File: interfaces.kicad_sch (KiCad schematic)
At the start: 125 parts, among them J3 USB-Micro-B_Amphenol_10118192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, J6 PinHeader_2x7_P2mm_Drill0.9mm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, J7 PinHeader_1x6_P2.54mm_Drill1.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, U1 MTFC16GAPALNA-AIT, U14 XC7A100T-FGG484, U17 USB3300-EZK-TR, U18 USB3300-EZK-TR, U19 FT4232H_QFN, U21 LSF0108RKSR, U22 LSF0101DRYR, U23 Oscillator_24MHz_ASEMB, U24 Oscillator_24MHz_ASEMB, U6 NVT2008BQ,115, Y1 Resonator_12MHz_ABM8G

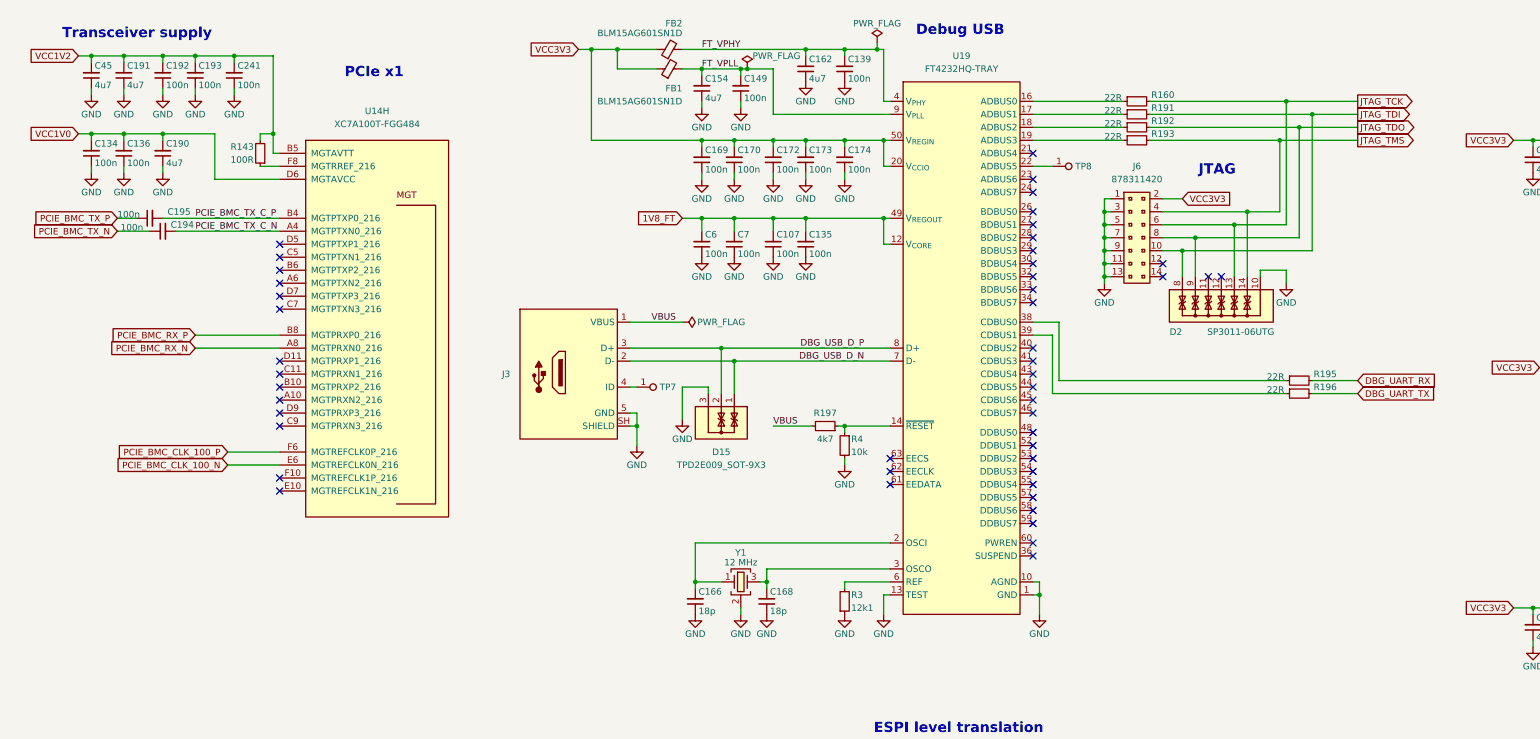
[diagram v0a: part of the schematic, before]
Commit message: [#68236] Update symbols and footprints, clean ERC and DRC
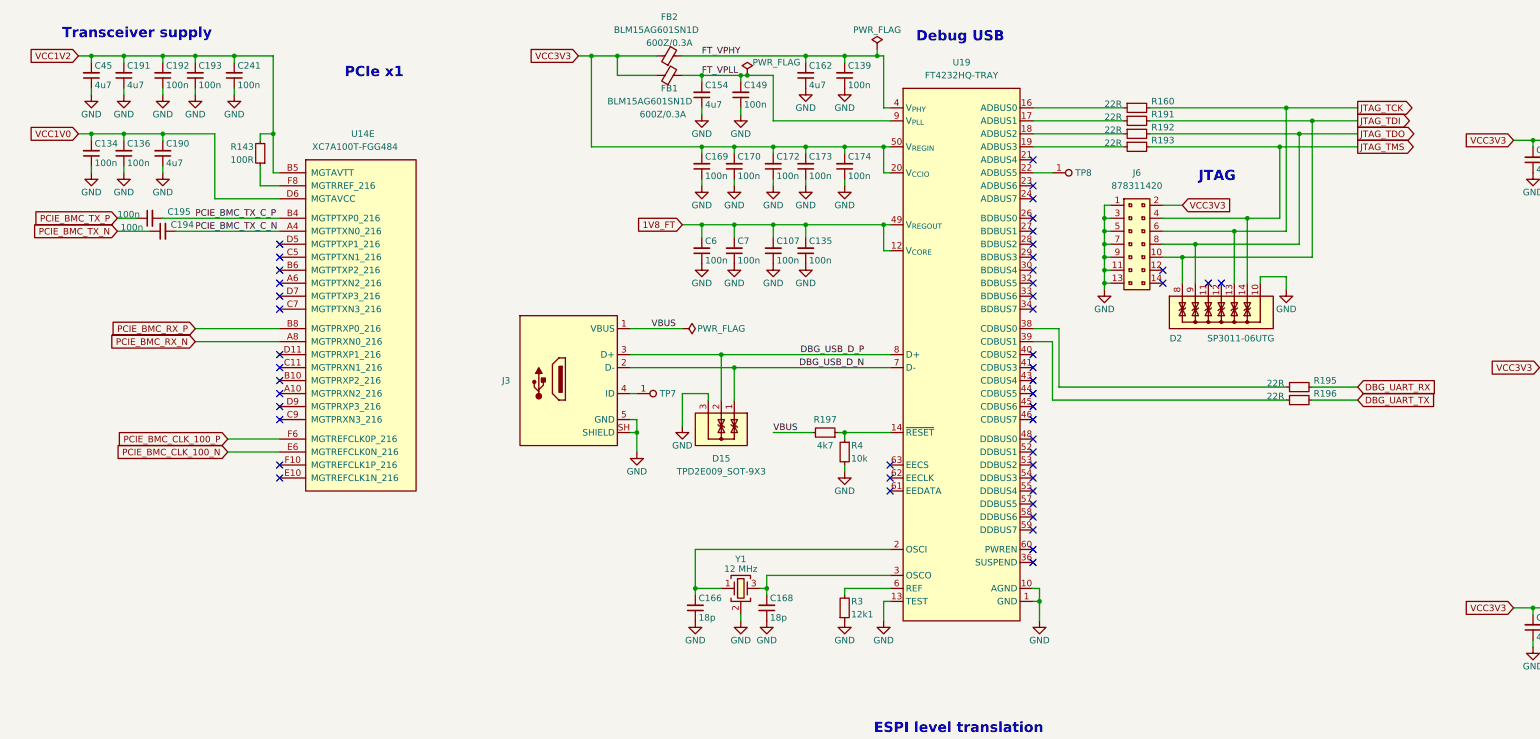
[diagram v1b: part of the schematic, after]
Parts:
- C134, C136, C17, C186, C187, C189, C192, C193, C194, C195, C223, C224, C229, C230, C231, C232, C241, C39: Public (none) -> False
- FB1, FB2: Val (none) -> 600Z/0.3A
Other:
- moved on the sheet: C107, C135, C139, C149, C154, C162, C166, C168, C169, C170, C172, C173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

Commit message: [#82378] Project refresh 81589
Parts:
- U21: DNP DNP -> (none)
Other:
- moved on the sheet: C4, C5

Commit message: pcb layout progress
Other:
- note added: "SFEM016GB1ED1TO-I-5E-311-STD (Drop in Replacement)"
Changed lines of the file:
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@@
 		(rev "1.1.3")
+	)
+	(text "SFEM016GB1ED1TO-I-5E-311-STD (Drop in Replacement)\n"
+		(exclude_from_sim no)
+		(at 89.154 227.33 0)
+		(effects
+			(font
+				(size 1.27 1.27)
+			)
+		)
 	)
 	(text "USB CLIENT"

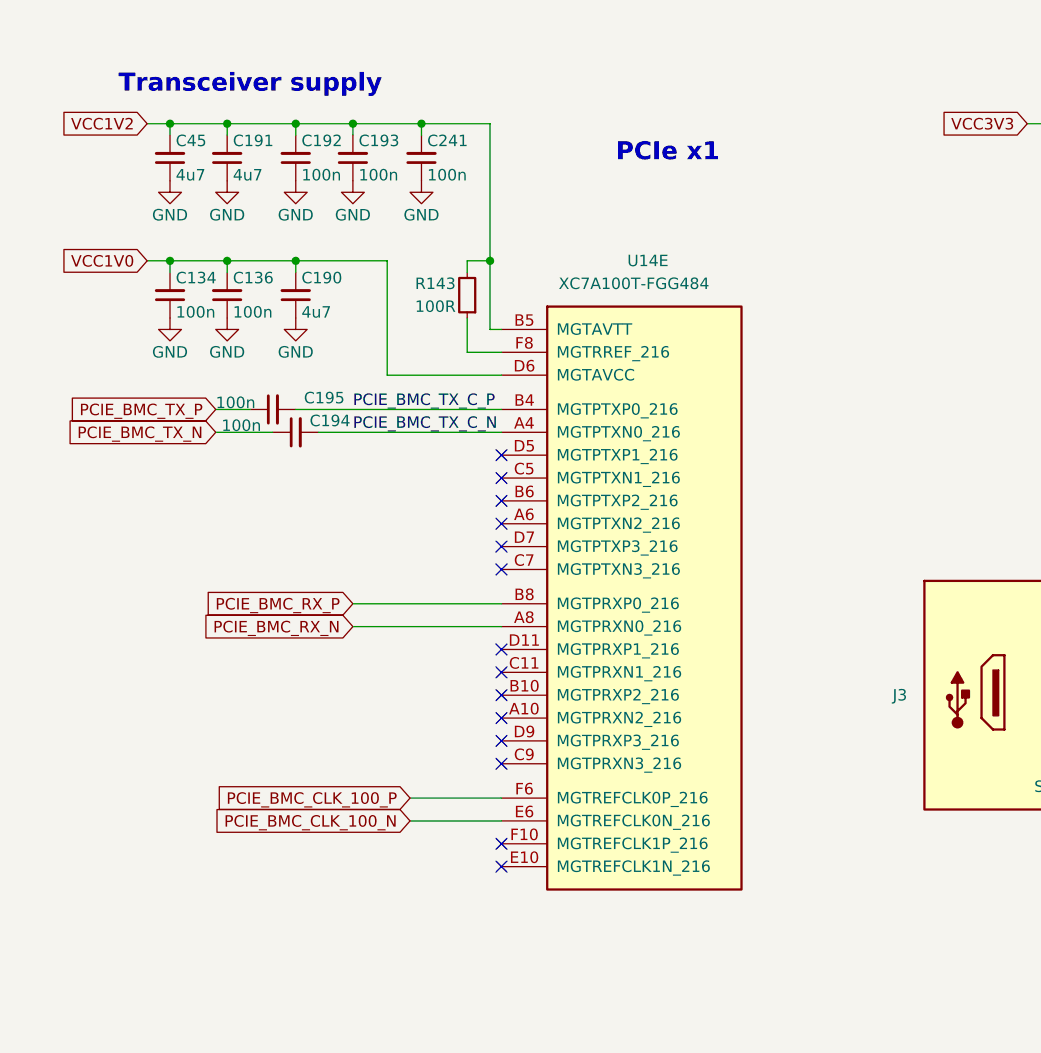
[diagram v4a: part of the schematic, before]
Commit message: a lot of routing and almost all caps of the fpga are placed down
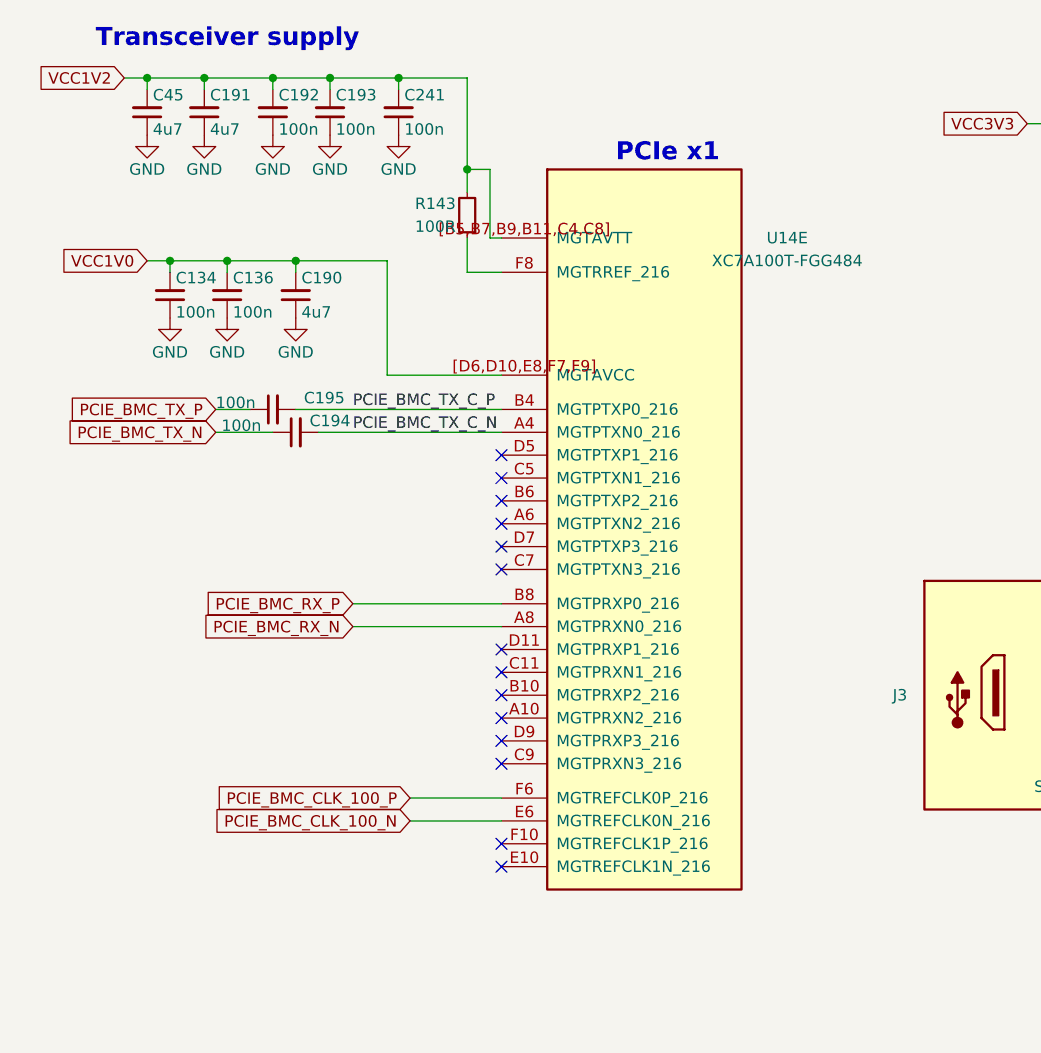
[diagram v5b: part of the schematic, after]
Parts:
- C10, C107, C11, C12, C13, C134, C135, C136, C139, C149, C154, C162, C166, C168, C169, C17, C170, C172, C173, C174, C177, C18, C183, C184, C185, C186, C187, C188, C189, C19, C192, C193, C194, C195, C20, C21, C22, C222, C223, C224, C229, C23, C230, C231, C232, C24, C241, C245, C246, C247, C248, C249, C25, C251, C252, C253, C254, C26, C39, C4, C5, C6, C7: footprint antmicro-footprints:C_0402_1005Metric -> Capacitor_SMD:C_0402_1005Metric
- C190, C191, C45: footprint antmicro-footprints:C_0603_1608Metric -> Capacitor_SMD:C_0603_1608Metric; MPN C1608X5R1V475M080AC -> C0603C475K9PAC; Manufacturer TDK -> KEMET
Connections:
- net VCC1V0: now also U14.[D6,D10,E8,F7,F9] (MGTAVCC); no longer U14.D10 (MGTAVCC), U14.D6 (MGTAVCC), U14.E8 (MGTAVCC), U14.F7 (MGTAVCC), U14.F9 (MGTAVCC)
- net VCC1V2: now also U14.[B5,B7,B9,B11,C4,C8] (MGTAVTT); no longer U14.B11 (MGTAVTT), U14.B5 (MGTAVTT), U14.B7 (MGTAVTT), U14.B9 (MGTAVTT), U14.C4 (MGTAVTT), U14.C8 (MGTAVTT)
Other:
- moved on the sheet: C191, C192, C193, C241, C45, R143, U14E

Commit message: bom changes
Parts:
- removed R197: R_4k7_0402, antmicro-footprints:R_0402_1005Metric, symbol antmicroResistors0402:R_4k7_0402
- removed R4: R_10k_0402, antmicro-footprints:R_0402_1005Metric, symbol antmicroResistors0402:R_10k_0402
- added C258: C_4u7_0402, Capacitor_SMD:C_0402_1005Metric, symbol antmicroCapacitors0402:C_4u7_0402
- added C261: C_100n_0402, Capacitor_SMD:C_0402_1005Metric, symbol antmicroCapacitors0402:C_100n_0402
- added R210, R211, R212, R213, R214: R_Small, Resistor_SMD:R_0402_1005Metric, symbol Device:R_Small
- added TP15, TP16, TP9: TestPoint, TestPoint:TestPoint_Pad_D1.0mm, symbol Connector:TestPoint
- added U26: FT2232HQ, Package_DFN_QFN:QFN-64-1EP_9x9mm_P0.5mm_EP4.35x4.35mm, symbol Interface_USB:FT2232HQ
- added U27: 93LCxxBxxOT, Package_TO_SOT_SMD:SOT-23-6, symbol Memory_EEPROM:93LCxxBxxOT
- J6: MPN 878311420 -> 87831-1420
- R10, R11: MPN ERJ2GE0R00X -> RC0402JR-7D0RL; Manufacturer Panasonic -> YAGEO
- U1: value MTFC16GAPALNA-AIT -> SFEM016GB1ED1TO-I-5E-311-STD; MPN MTFC16GAPALNA-AIT -> SFEM016GB1ED1TO-I-5E-311-STD; Manufacturer Micron Technology -> Swissbit
- U19: now left out of the parts list
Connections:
- net DBG_UART_RX: now also TP15.1
- net DBG_UART_TX: now also TP9.1
- net DBG_USB_D_N: now also U26.7 (DM); no longer U19.7 (D-)
- net DBG_USB_D_P: now also U26.8 (DP); no longer U19.8 (D+)
- net FT_VPHY: now also U26.4 (VPHY); no longer U19.4 (V_{PHY})
- net FT_VPLL: now also U26.9 (VPLL); no longer U19.9 (V_{PLL})
- net GND: now also C258.1, C261.1, TP16.1, U26.10 (AGND), U26.13 (TEST), U26.[1,5,11,15,25,35,47,51,65] (GND), U27.2 (GND); no longer U19.1 (GND), U19.10 (AGND), U19.11 (GND), U19.13 (TEST), U19.15 (GND), U19.25 (GND), U19.35 (GND), U19.47 (GND), U19.5 (GND), U19.51 (GND), U19.65 (GND)
- net VCC3V3: now also C261.2, R211.2, R212.2, R213.2, R214.2, U26.50 (VREGIN), U26.[20,31,42,56] (VCCIO), U27.6 (VCC); no longer U19.20 (V_{CCIO}), U19.31 (V_{CCIO}), U19.42 (V_{CCIO}), U19.50 (V_{REGIN}), U19.56 (V_{CCIO})
- net at U19.6 (REF): no longer R3.2
- net at C166.2, Y1.1: now also U26.2 (OSCI); no longer U19.2 (OSCI)
- net at C168.2, Y1.3: now also U26.3 (OSCO); no longer U19.3 (OSCO)
- net at R160.1: now also U26.16 (ADBUS0); no longer U19.16 (ADBUS0)
- net at U19.17 (ADBUS1): no longer R191.1
- net at U19.18 (ADBUS2): no longer R192.1
- net at U19.19 (ADBUS3): no longer R193.1
- net at U19.22 (ADBUS5): no longer TP8.1
- net at R195.1: now also U26.38 (BDBUS0); no longer U19.38 (CDBUS0)
- net at U19.39 (CDBUS1): no longer R196.1
- net 1V8_FT renamed V_Regout
- net V_Regout: now also C258.2, U26.49 (VREGOUT), U26.[12,37,64] (VCORE); no longer U19.12 (V_{CORE}), U19.37 (V_{CORE}), U19.49 (V_{REGOUT}), U19.64 (V_{CORE})
- new net: R214.1, U26.14 (~{RESET})
- new net: R212.1, U26.62 (EECLK), U27.4 (CLK)
- new net: R210.1, R213.1, U27.1 (DO)
- new net: R210.2, U26.61 (EEDATA), U27.3 (DI)
- new net: U19.1 (GND), U19.11 (GND), U19.15 (GND), U19.25 (GND), U19.35 (GND), U19.47 (GND), U19.5 (GND), U19.51 (GND), U19.65 (GND)
- new net: U19.12 (V_{CORE}), U19.37 (V_{CORE}), U19.64 (V_{CORE})
- new net: U19.20 (V_{CCIO}), U19.31 (V_{CCIO}), U19.42 (V_{CCIO}), U19.56 (V_{CCIO})
- new net: R211.1, U26.63 (EECS), U27.5 (CS)
- new net: R3.2, U26.6 (REF)
- new net: R191.1, U26.17 (ADBUS1)
- new net: R192.1, U26.18 (ADBUS2)
- new net: R193.1, U26.19 (ADBUS3)
- new net: TP8.1, U26.22 (ADBUS5)
- new net: R196.1, U26.39 (BDBUS1)
- no-connect marks 56 -> 105

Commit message: version 1.0 complete
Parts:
- R143: MPN CR0402-FX-1000GLF -> RC0402FR-7D100RL; Manufacturer Bourns -> YAGEO
- R160, R191, R192, R193, R195, R196, R9: MPN CR0402-FX-22R0GLF -> RC0402FR-7D22RL; Manufacturer Bourns -> YAGEO
- R210: value R_Small -> R_2k2_0402; MPN (none) -> AC0402FR-7D2K2L; Manufacturer (none) -> YAGEO; Val (none) -> 2k2
- R211, R212, R213: value R_Small -> R_10k_0402; MPN (none) -> CR0402AFX-1002GAS; Manufacturer (none) -> Bourns
- R214: value R_Small -> R_1k_0402; MPN (none) -> CR0402-FX-1001GLF; Manufacturer (none) -> Bourns; Val (none) -> 1k
- U14: MPN XC7A100T-FGG484 -> XC7A100T-2FGG484C
- U26: MPN (none) -> FT2232HQ-REEL; Manufacturer (none) -> FTDI Chip
